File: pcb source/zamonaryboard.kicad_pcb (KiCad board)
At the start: 2 copper layers, 52.3 x 40.6 mm, 21 parts, among them J1 USB_C_Receptacle_USB2.0_14P, SW1 SW_Push, U1 ESP32-S2, U2 ME6211C33M5, Y1 Crystal_GND24

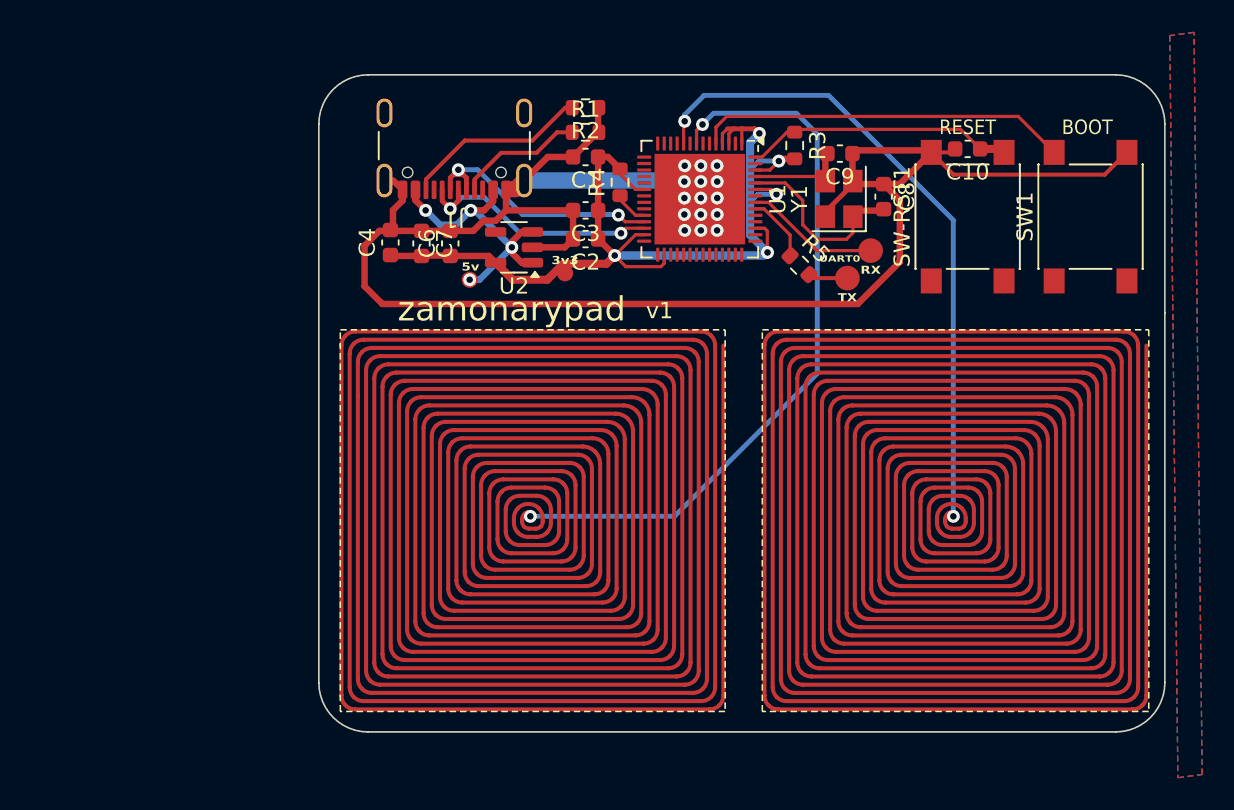
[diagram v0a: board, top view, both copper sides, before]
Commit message: Flipped type-c port and main buttons to the back side, changed reset/boot button to be slimmer, initial new branch commit
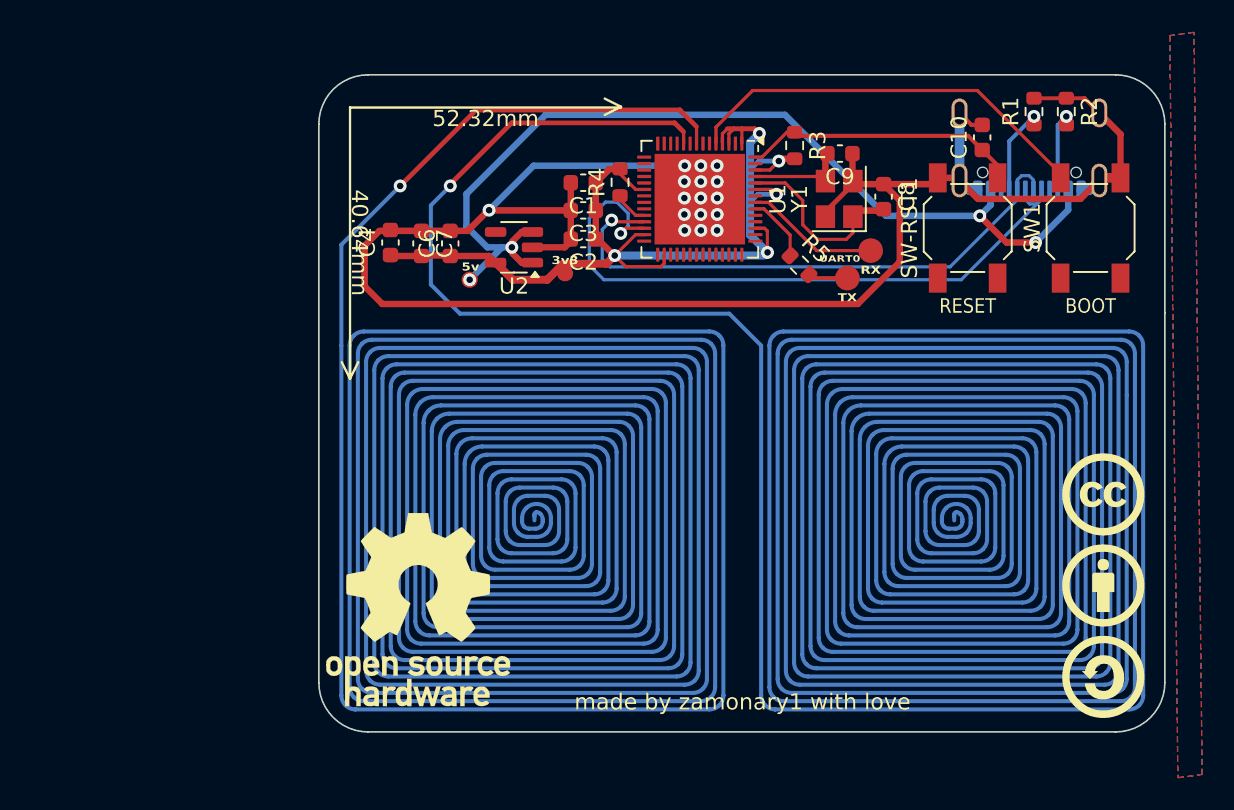
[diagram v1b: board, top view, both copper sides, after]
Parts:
- J1: moved to B.Cu
- REF**: moved to F.Cu
- SW-RST1, SW1: footprint Button_Switch_SMD:SW_Push_1P1T_NO_6x6mm_H9.5mm -> Button_Switch_SMD:SW_SPST_SKQG_WithoutStem
- moved REF** 39.6 mm to (125.0, 104.7), turned to 0 degrees
- moved J1 35.6 mm to (162.8, 75.1), turned to 0 degrees
- moved R2 29.7 mm to (165.1, 73.9), turned to -90 degrees
- moved R1 27.8 mm to (163.1, 73.9), turned to 90 degrees
- moved C1 1.60 mm to (135.2, 78.3)
- moved C10 1.15 mm to (159.9, 75.5), turned to 90 degrees
- moved SW-RST1 0.70 mm to (159.0, 81.1)
- moved SW1 0.70 mm to (166.6, 81.1)
- moved C2 0.14 mm to (135.2, 81.8)
- moved C3 0.14 mm to (135.2, 80.0)
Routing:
- net VBUS: track 18.0 -> 58.4 mm
- net D+: track 15.9 -> 41.5 mm, vias 2 -> 1
- net D-: track 15.5 -> 35.3 mm, vias 2 -> 1
- net BTN1: track 1142.9 -> 1130.6 mm, vias 2 -> 1
- net Net-(J1-CC2): track 11.5 -> 4.76 mm, vias 0 -> 1
- net BTN2: track 1137.9 -> 1143.1 mm, vias 2 -> 1
- net Net-(J1-CC1): track 7.94 -> 5.17 mm, vias 0 -> 1
- net Net-(U1-GPIO0/BOOT): track 23.1 -> 25.7 mm
- net +3V3: track 64.5 -> 63.3 mm
- net GND: track 114.7 -> 116.0 mm, vias 15 -> 16
- net Net-(U1-CHIP_PU/RESET): track 16.7 -> 17.3 mm

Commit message: WS2812 2020 on the pcb! Not necesseary for proper work
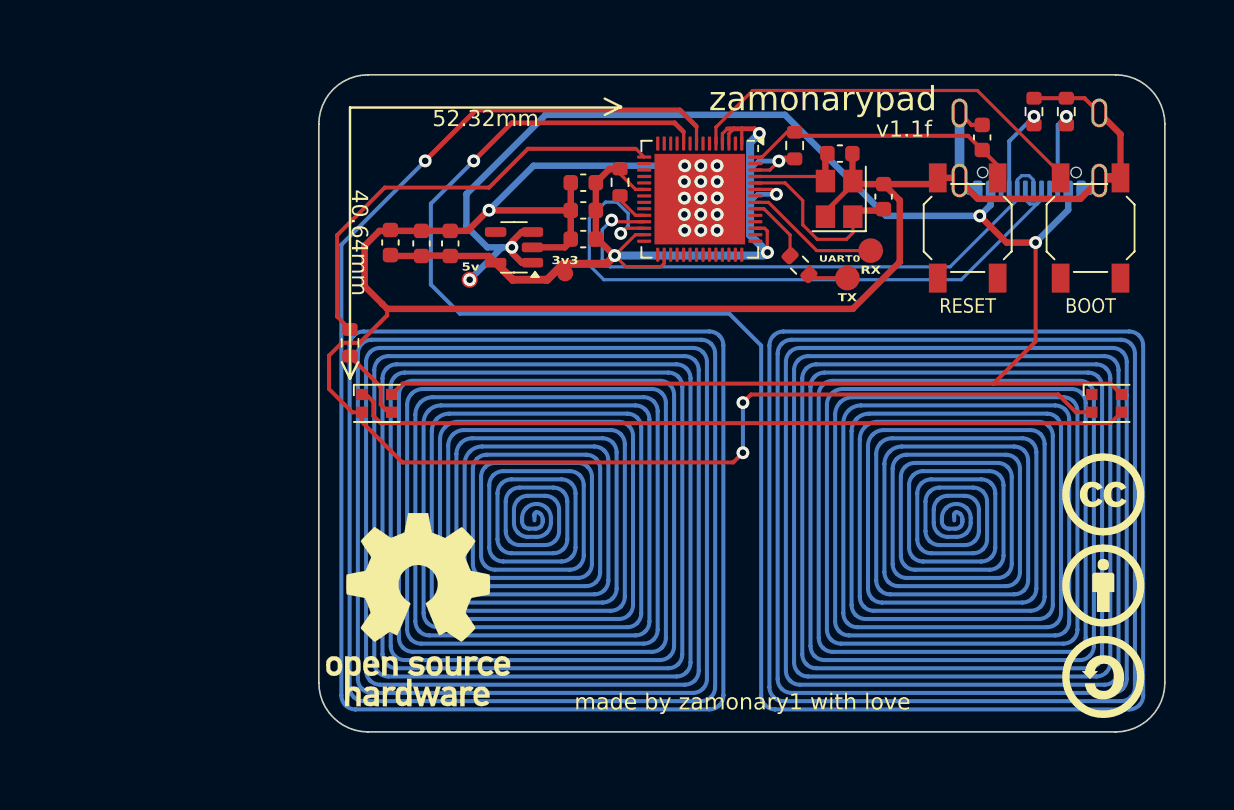
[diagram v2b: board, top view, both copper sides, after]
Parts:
- added D1: WS2812B-2020, LED_SMD:LED_WS2812B-2020_PLCC4_2.0x2.0mm, F.Cu at (167.6, 91.9)
- added D2: WS2812B-2020, LED_SMD:LED_WS2812B-2020_PLCC4_2.0x2.0mm, F.Cu at (122.5, 91.9)
- added R6: 500, Resistor_SMD:R_0603_1608Metric, F.Cu at (120.8, 88.2)
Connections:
- U1 pad 15: unconnected-(U1-GPIO10/ADC1_CH9-Pad15) -> aRGB_pin
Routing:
- net GND: track 116.0 -> 176.7 mm, vias 16 -> 18
- net VBUS: track 58.4 -> 113.9 mm
- net Net-(D1-DIN): track 0.00 -> 48.5 mm
- net aRGB_pin: track 0.00 -> 27.6 mm
- net Net-(D2-DIN): track 0.00 -> 4.66 mm
- removed copper zone on B.Cu, net (none)
- removed copper zone on F.Cu, net (none)
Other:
- outline, holes or cut-outs redrawn
- board text added: "v1.1f"
- board text removed: "v1"

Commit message: v1.2-f, added WS2812-2020 argb leds on the backside of the board (unnecesseary), improvements to pcb routing
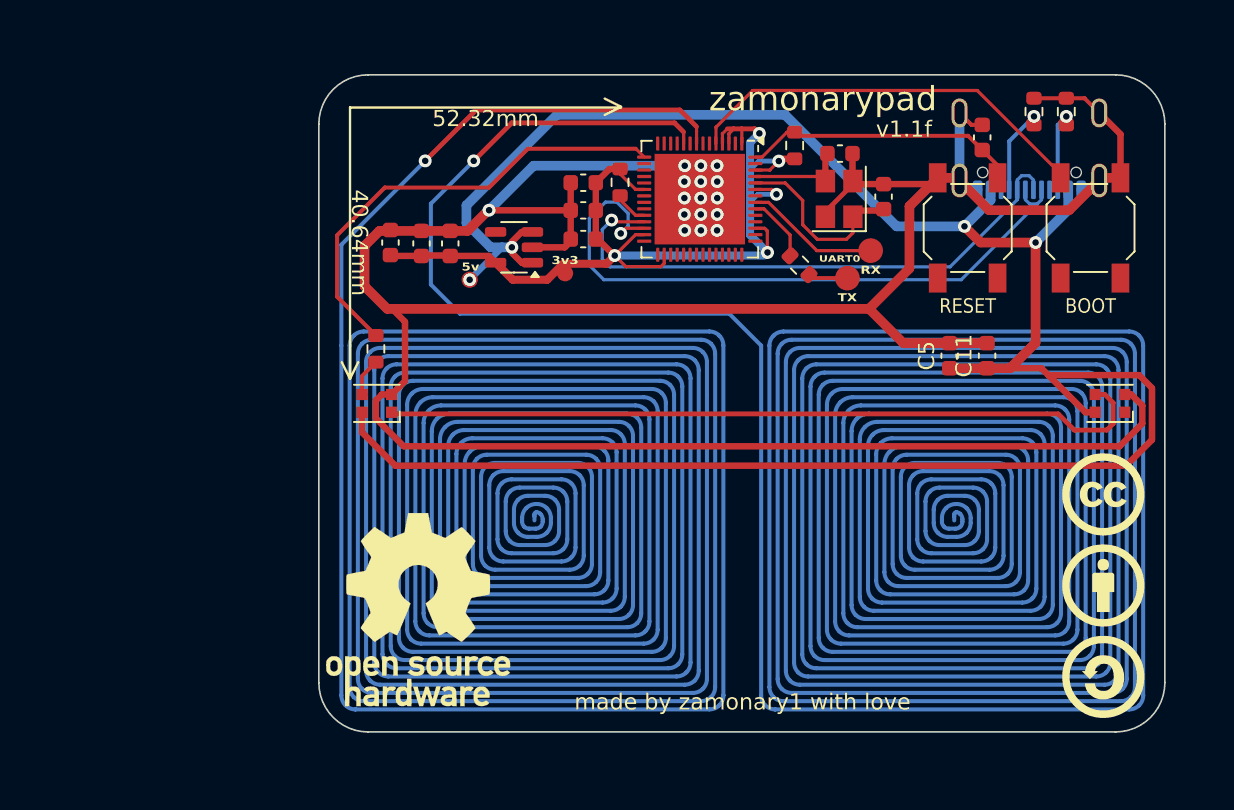
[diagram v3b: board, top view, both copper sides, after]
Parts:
- added C11: 100nF, Capacitor_SMD:C_0603_1608Metric, F.Cu at (160.2, 89.0)
- added C5: 1uF, Capacitor_SMD:C_0603_1608Metric, F.Cu at (157.9, 89.0)
- R5, R6: value 500 -> 480
- moved R6 1.64 mm to (122.4, 88.6)
- moved D1 0.21 mm to (167.8, 91.9), turned to 180 degrees
- turned D2 to 180 degrees
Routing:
- net VBUS: track 113.9 -> 139.0 mm
- net GND: track 176.7 -> 185.9 mm, vias 18 -> 16
- net Net-(D2-DIN): track 4.66 -> 2.60 mm
- net aRGB_pin: track 27.6 -> 28.6 mm

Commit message: Added a cut between sensitive pads to give some tactile feedback to the board.
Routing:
- net GND: track 185.9 -> 146.0 mm
- net VBUS: track 139.0 -> 152.0 mm
- net BTN2: track 1143.1 -> 1144.2 mm
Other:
- outline, holes or cut-outs redrawn
- board text added: "v1.2f"
- board text removed: "v1.1f"

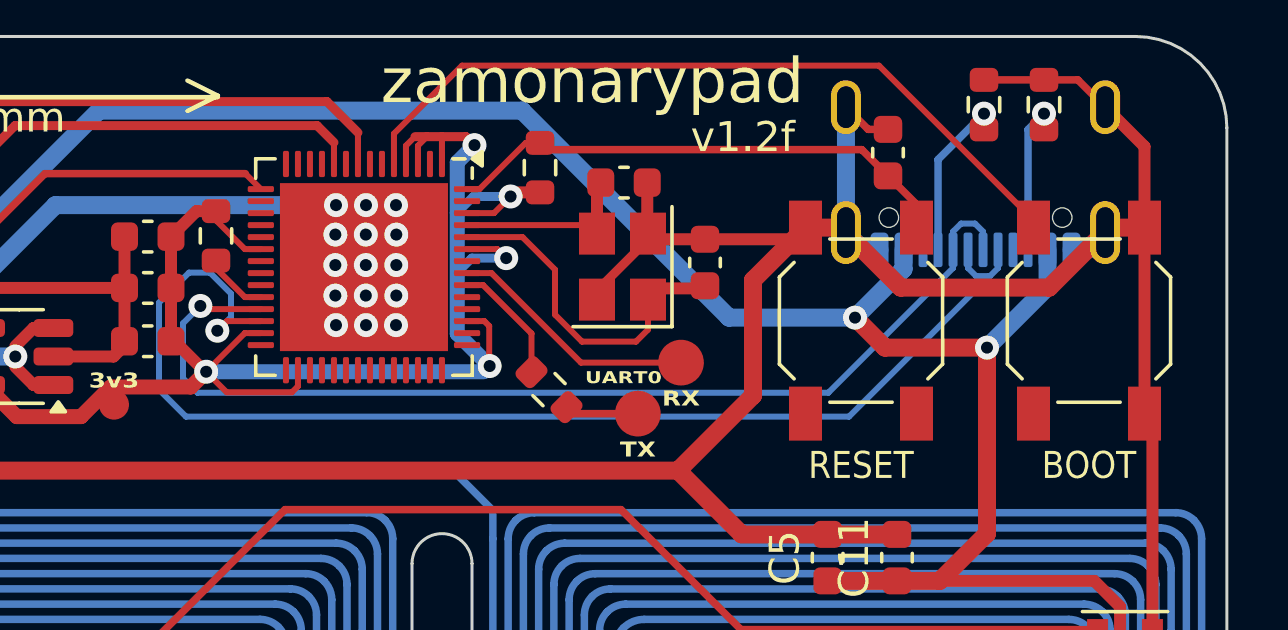
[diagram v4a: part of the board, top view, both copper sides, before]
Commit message: Firmware code cleanup, add support for addressible LEDs.
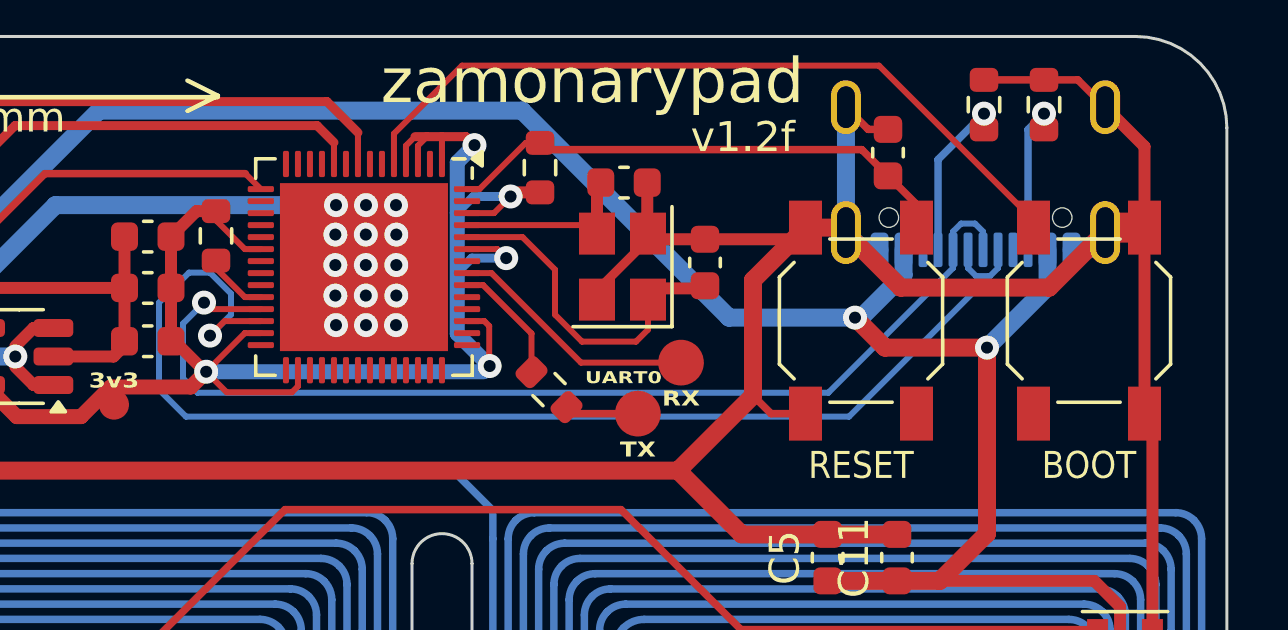
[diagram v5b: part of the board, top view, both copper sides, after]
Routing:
- net GND: track 146.0 -> 148.0 mm
- net D+: track 41.5 -> 42.0 mm
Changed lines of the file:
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@@
 			(layer "F.SilkS"
 				(type "Top Silk Screen")
+				(color "Black")
 			)
 			(layer "F.Paste"
@@
 			(layer "F.Mask"
 				(type "Top Solder Mask")
+				(color "White")
 				(thickness 0.01)
 			)
@@
 			(layer "dielectric 1"
 				(type "core")
+				(color "FR4 natural")
 				(thickness 1.51)
 				(material "FR4")
@@
 			(layer "B.Mask"
 				(type "Bottom Solder Mask")
+				(color "White")
 				(thickness 0.01)
 			)
@@
 			(layer "B.SilkS"
 				(type "Bottom Silk Screen")
+				(color "Black")
 			)
 			(copper_finish "None")
@@
 			(drillshape 0)
 			(scaleselection 1)
-			(outputdirectory "../../pcb-export/v1.1-f/")
+			(outputdirectory "../../pcb-export/zp-v1.2-f/")
 		)
 	)
@@
 		(start 167.275 78)
 		(end 168.45 78)
-		(width 0.6)
+		(width 1)
 		(layer "F.Cu")
 		(net 1)
@@
 	)
 	(segment
+		(start 157.15 84.2)
+		(end 156 84.2)
+		(width 0.25)
+		(layer "F.Cu")
+		(net 1)
+	)
+	(segment
+		(start 156 84.2)
+		(end 155.4 83.6)
+		(width 0.25)
+		(layer "F.Cu")
+		(net 1)
+	)
+	(segment
 		(start 157.15 78)
 		(end 158.325 78)
@@
 	)
 	(segment
-		(start 137.54353 81.437012)
-		(end 137.864542 81.116)
+		(start 137.3 81.6)
+		(end 137.784 81.116)
 		(width 0.2)
 		(layer "F.Cu")
@@
 	)
 	(segment
-		(start 137.864542 81.116)
+		(start 137.784 81.116)
 		(end 138.9945 81.116)
 		(width 0.2)
@@
 	)
 	(via
-		(at 137.54353 81.437012)
+		(at 137.3 81.6)
 		(size 0.8)
 		(drill 0.4)
@@
 	)
 	(segment
-		(start 138 80.2)
-		(end 137.3 79.5)
+		(start 137.3 79.5)
+		(end 136.6 79.5)
 		(width 0.2)
 		(layer "B.Cu")
@@
 	)
 	(segment
-		(start 163.568 79.34741)
-		(end 163.568 78.74)
+		(start 135.6 80.5)
+		(end 135.6 83.4)
 		(width 0.2)
 		(layer "B.Cu")
@@
 	)
 	(segment
-		(start 162.83559 79.615)
+		(start 163.285 79.615)
 		(end 163.30041 79.615)
 		(width 0.2)
@@
 	)
 	(segment
-		(start 136.5 84.3)
-		(end 158.6 84.3)
+		(start 163.568 79.34741)
+		(end 163.568 78.74)
 		(width 0.2)
 		(layer "B.Cu")
@@
 	)
 	(segment
-		(start 137.54353 81.437012)
-		(end 138 80.980542)
+		(start 162.83559 79.615)
+		(end 163.30041 79.615)
 		(width 0.2)
 		(layer "B.Cu")
@@
 	)
 	(segment
+		(start 137.3 81.6)
+		(end 138 80.9)
+		(width 0.2)
+		(layer "B.Cu")
+		(net 3)
+	)
+	(segment
 		(start 162.568 79.34741)
 		(end 162.83559 79.615)
@@
 	)
 	(segment
-		(start 138 80.980542)
-		(end 138 80.2)
+		(start 138 80.2)
+		(end 137.3 79.5)
 		(width 0.2)
 		(layer "B.Cu")
@@
 	)
 	(segment
-		(start 135.6 80.5)
-		(end 135.6 83.4)
+		(start 135.6 83.4)
+		(end 136.5 84.3)
 		(width 0.2)
 		(layer "B.Cu")
@@
 	)
 	(segment
-		(start 137.3 79.5)
-		(end 136.6 79.5)
+		(start 136.5 84.3)
+		(end 158.6 84.3)
 		(width 0.2)
 		(layer "B.Cu")
@@
 	)
 	(segment
-		(start 135.6 83.4)
-		(end 136.5 84.3)
+		(start 138 80.9)
+		(end 138 80.2)
 		(width 0.2)
 		(layer "B.Cu")
@@
 	)
 	(segment
-		(start 163.285 79.615)
-		(end 163.30041 79.615)
-		(width 0.2)
-		(layer "B.Cu")
-		(net 3)
-	)
-	(segment
 		(start 159.8 82)
 		(end 158.8 81)
@@
 	)
 	(segment
-		(start 160.418 78.74)
-		(end 160.418 79.382)
-		(width 0.6)
-		(layer "B.Cu")
-		(net 4)
-	)
-	(segment
 		(start 165.218 79.982)
 		(end 165.218 78.74)
@@
 	)
 	(segment
-		(start 160.418 79.382)
-		(end 158.8 81)
+		(start 163.2 82)
+		(end 165.218 79.982)
 		(width 0.6)
 		(layer "B.Cu")
@@
 	)
 	(segment
-		(start 163.2 82)
-		(end 165.218 79.982)
+		(start 160.418 78.74)
+		(end 160.418 79.582)
 		(width 0.6)
 		(layer "B.Cu")
@@
 	)
 	(segment
+		(start 159 81)
+		(end 158.8 81)
+		(width 0.6)
+		(layer "B.Cu")
+		(net 4)
+	)
+	(segment
+		(start 160.418 79.582)
+		(end 159 81)
+		(width 0.6)
+		(layer "B.Cu")
+		(net 4)
+	)
+	(segment
 		(start 130.204 82.296)
 		(end 129.496 82.296)
@@
 	)
 	(segment
-		(start 136.979117 80.611516)
-		(end 137.083601 80.716)
+		(start 137.316 80.716)
+		(end 138.9945 80.716)
 		(width 0.2)
 		(layer "F.Cu")
@@
 	)
 	(segment
-		(start 137.083601 80.716)
-		(end 138.9945 80.716)
+		(start 137.1 80.5)
+		(end 137.316 80.716)
 		(width 0.2)
 		(layer "F.Cu")
@@
 	)
 	(via
-		(at 136.979117 80.611516)
+		(at 137.1 80.5)
 		(size 0.8)
 		(drill 0.4)
@@
 	)
 	(segment
-		(start 136.88269 83.504)
-		(end 136.4 83.02131)
+		(start 157.91141 83.504)
+		(end 162.068 79.34741)
 		(width 0.2)
 		(layer "B.Cu")
@@
 	)
 	(segment
-		(start 157.91141 83.504)
-		(end 136.88269 83.504)
+		(start 163.068 78.13259)
+		(end 163.068 78.74)
 		(width 0.2)
 		(layer "B.Cu")
@@
 	)
 	(segment
-		(start 163.068 78.13259)
-		(end 163.068 78.74)
+		(start 136.4 83.02131)
+		(end 136.88269 83.504)
 		(width 0.2)
 		(layer "B.Cu")
@@
 	)
 	(segment
-		(start 162.068 79.34741)
-		(end 157.91141 83.504)
+		(start 137.1 80.5)
+		(end 136.4 81.2)
 		(width 0.2)
 		(layer "B.Cu")
@@
 	)
 	(segment
-		(start 136.4 83.02131)
-		(end 136.4 81.190633)
+		(start 162.068 79.34741)
+		(end 162.068 78.74)
 		(width 0.2)
 		(layer "B.Cu")
@@
 	)
 	(segment
-		(start 162.068 78.74)
-		(end 162.068 79.34741)
+		(start 136.4 81.2)
+		(end 136.4 83.02131)
 		(width 0.2)
 		(layer "B.Cu")
@@
 	)
 	(segment
+		(start 136.88269 83.504)
+		(end 157.91141 83.504)
+		(width 0.2)
+		(layer "B.Cu")
+		(net 6)
+	)
+	(segment
 		(start 162.80041 77.865)
 		(end 163.068 78.13259)
@@
 		(width 0.2)
 		(layer "B.Cu")
-		(net 6)
-	)
-	(segment
-		(start 136.4 81.190633)
-		(end 136.979117 80.611516)
-		(width 0.2)
-		(layer "B.Cu")
